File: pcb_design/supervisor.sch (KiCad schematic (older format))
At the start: 15 parts, among them U5 7400-TSSOP, U6 SN74ALVC08PWR, U7 SN74ALVC08PWR, U8 SN74AUP1G74

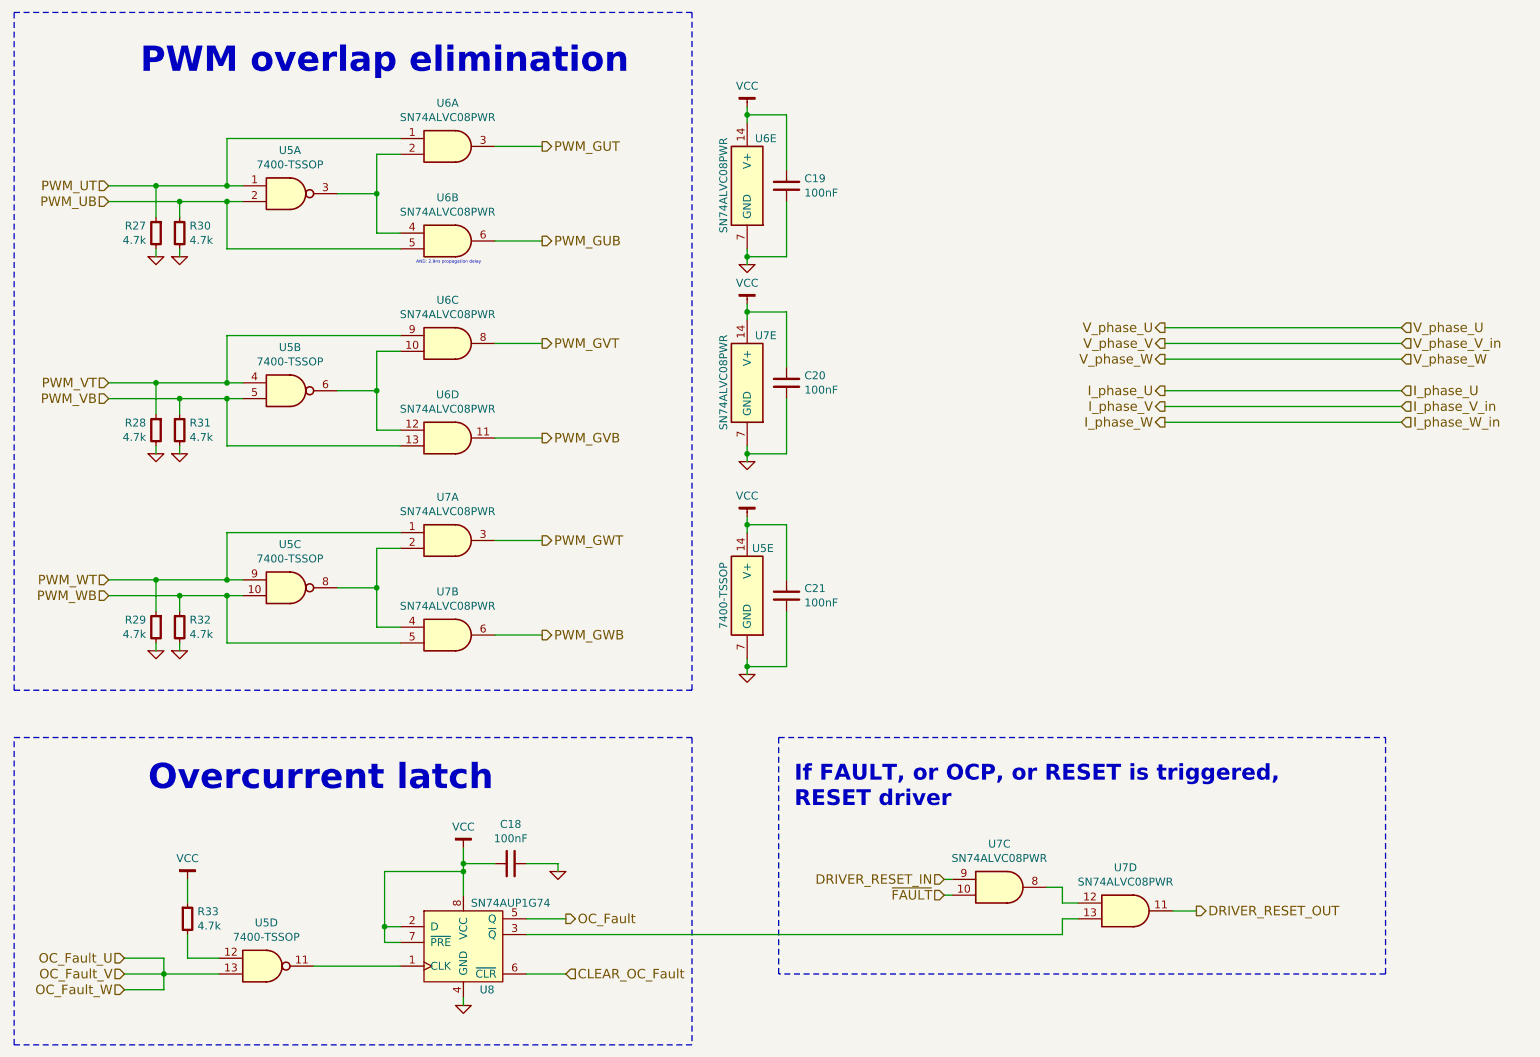
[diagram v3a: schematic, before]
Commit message: Added lp filters, fuses, tvs and power symbols
Signed-off-by: Marcos Chaparro <mchaparro@paltatech.com>
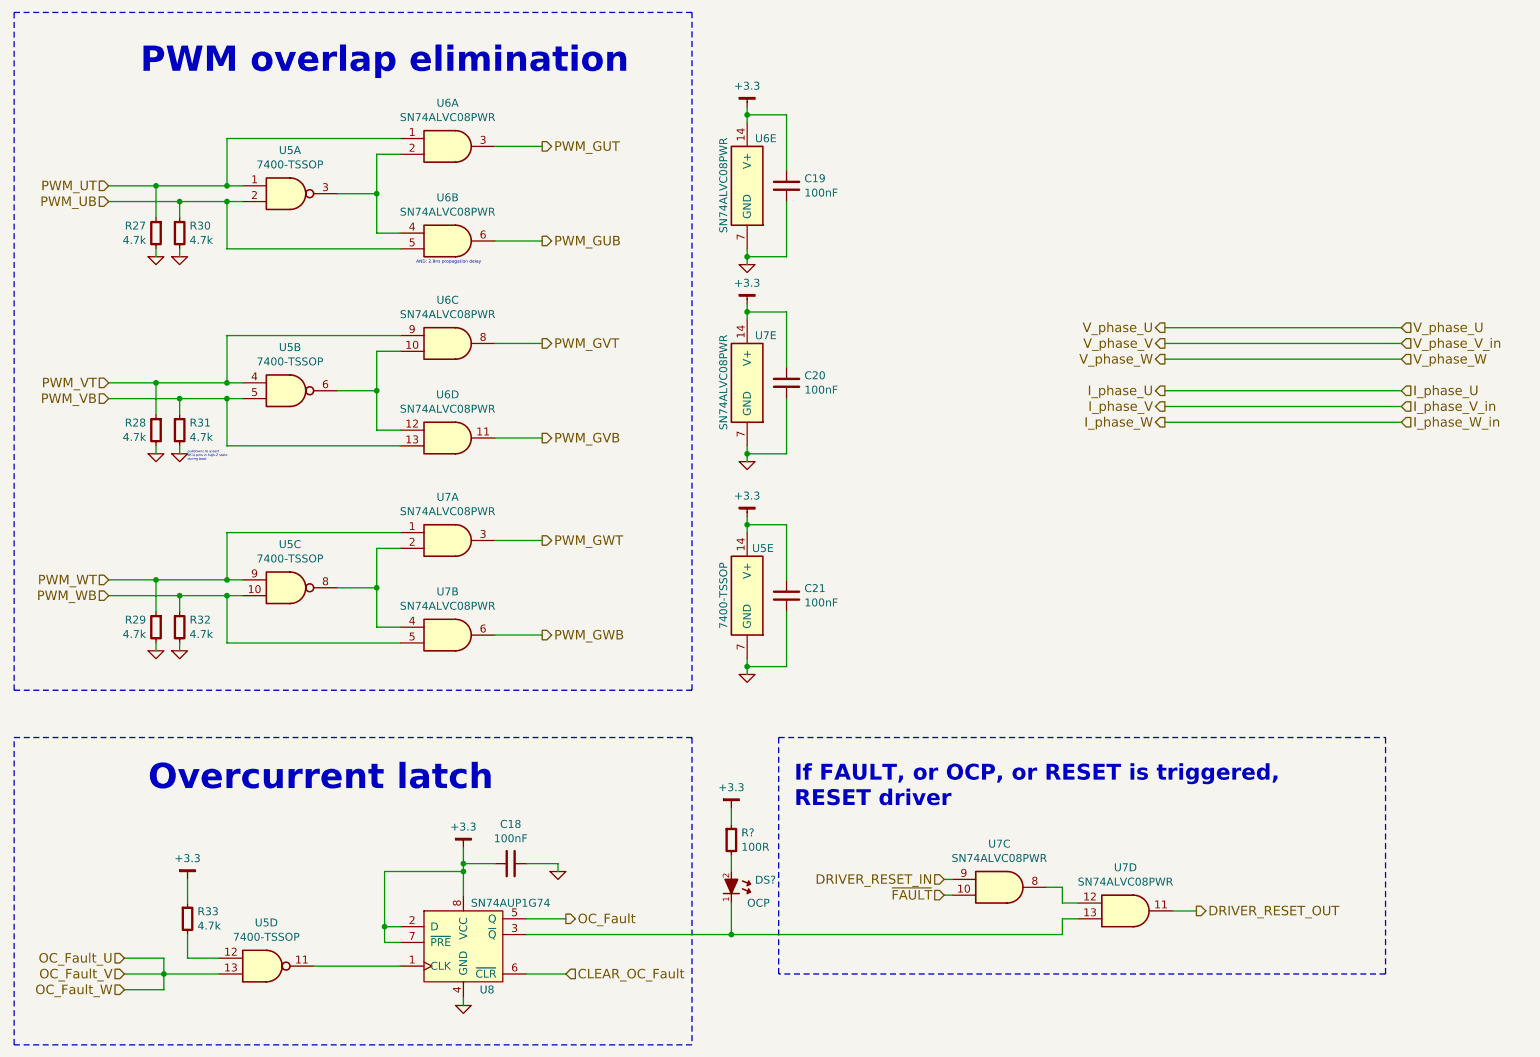
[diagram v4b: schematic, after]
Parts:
- added DS?: OCP, smd-semi:LED-0603, symbol LED-0603
- added R?: 100R, IPC7351-Nominal:RESC1608X50, symbol R-0603
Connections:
- net at U7.13 (D2D), U8.3 (~Q): now also DS?.1 (K)
- net VCC renamed +3.3
- net +3.3: now also R?.1
- new net: DS?.2 (A), R?.2
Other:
- note added: "pulldowns to assert\nMCU pins in high-Z state\nduring boot"
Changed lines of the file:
@@
 Wire Notes Line
 	5800 6950 5800 5450
-$Comp
-L VCC #PWR?
-U 1 1 588980B5
-P 3800 6150
-AR Path="/5886DA84/588980B5" Ref="#PWR?"  Part="1"
-AR Path="/588C2790/588980B5" Ref="#PWR?"  Part="1"
-AR Path="/5888D059/588980B5" Ref="#PWR76"  Part="1"
-F 0 "#PWR76" H 3800 6200 30  0001 C CNN
-F 1 "VCC" H 3800 6283 50  0000 C CNN
-F 2 "" H 3800 6150 60  0000 C CNN
-F 3 "" H 3800 6150 60  0000 C CNN
-	1    3800 6150
-	1    0    0    -1
-$EndComp
-$Comp
-L VCC #PWR?
-U 1 1 58898103
-P 2050 6350
-AR Path="/5886DA84/58898103" Ref="#PWR?"  Part="1"
-AR Path="/588C2790/58898103" Ref="#PWR?"  Part="1"
-AR Path="/5888D059/58898103" Ref="#PWR75"  Part="1"
-F 0 "#PWR75" H 2050 6400 30  0001 C CNN
-F 1 "VCC" H 2050 6483 50  0000 C CNN
-F 2 "" H 2050 6350 60  0000 C CNN
-F 3 "" H 2050 6350 60  0000 C CNN
-	1    2050 6350
-	1    0    0    -1
-$EndComp
-$Comp
-L VCC #PWR?
-U 1 1 588981CE
-P 5600 4050
-AR Path="/5886DA84/588981CE" Ref="#PWR?"  Part="1"
-AR Path="/588C2790/588981CE" Ref="#PWR?"  Part="1"
-AR Path="/5888D059/588981CE" Ref="#PWR83"  Part="1"
-F 0 "#PWR83" H 5600 4100 30  0001 C CNN
-F 1 "VCC" H 5600 4183 50  0000 C CNN
-F 2 "" H 5600 4050 60  0000 C CNN
-F 3 "" H 5600 4050 60  0000 C CNN
-	1    5600 4050
-	1    0    0    -1
-$EndComp
 Wire Wire Line
 	5600 4050 5600 4150
-$Comp
-L VCC #PWR?
-U 1 1 58898412
-P 5600 1450
-AR Path="/5886DA84/58898412" Ref="#PWR?"  Part="1"
-AR Path="/588C2790/58898412" Ref="#PWR?"  Part="1"
-AR Path="/5888D059/58898412" Ref="#PWR79"  Part="1"
-F 0 "#PWR79" H 5600 1500 30  0001 C CNN
-F 1 "VCC" H 5600 1583 50  0000 C CNN
-F 2 "" H 5600 1450 60  0000 C CNN
-F 3 "" H 5600 1450 60  0000 C CNN
-	1    5600 1450
-	1    0    0    -1
-$EndComp
 Wire Wire Line
 	5600 1450 5600 1550
-$Comp
-L VCC #PWR?
-U 1 1 588984F1
-P 5600 2700
-AR Path="/5886DA84/588984F1" Ref="#PWR?"  Part="1"
-AR Path="/588C2790/588984F1" Ref="#PWR?"  Part="1"
-AR Path="/5888D059/588984F1" Ref="#PWR81"  Part="1"
-F 0 "#PWR81" H 5600 2750 30  0001 C CNN
-F 1 "VCC" H 5600 2833 50  0000 C CNN
-F 2 "" H 5600 2700 60  0000 C CNN
-F 3 "" H 5600 2700 60  0000 C CNN
-	1    5600 2700
-	1    0    0    -1
-$EndComp
 Wire Wire Line
 	5600 2700 5600 2800
@@
 	1    0    0    -1
 $EndComp
+$Comp
+L LED-0603 DS?
+U 1 1 588B328E
+P 5500 6400
+F 0 "DS?" H 5650 6446 50  0000 L CNN
+F 1 "OCP" H 5600 6300 50  0000 L CNN
+F 2 "smd-semi:LED-0603" H -300 -550 50  0001 C CNN
+F 3 "" H -300 -400 60  0000 C CNN
+F 4 "LED RED [0603]" H -300 -650 60  0001 C CNN "BOM"
+	1    5500 6400
+	1    0    0    -1
+$EndComp
+$Comp
+L R-0603 R?
+U 1 1 588B34EA
+P 5500 6100
+F 0 "R?" H 5563 6146 50  0000 L CNN
+F 1 "100R" H 5563 6055 50  0000 L CNN
+F 2 "IPC7351-Nominal:RESC1608X50" H 5500 6100 50  0001 C CNN
+F 3 "" H 5500 6150 60  0000 C CNN
+F 4 "RES SMD 1k 5% [0603]" H 6250 6650 60  0001 C CNN "BOM"
+	1    5500 6100
+	1    0    0    -1
+$EndComp
+Wire Wire Line
+	5500 6200 5500 6300
+Wire Wire Line
+	5500 6500 5500 6700
+Connection ~ 5500 6700
+Wire Wire Line
+	5500 5900 5500 6000
+$Comp
+L +3.3 #PWR?
+U 1 1 588B453A
+P 5600 4050
+F 0 "#PWR?" H 5650 4100 30  0001 C CNN
+F 1 "+3.3" H 5600 4183 50  0000 C CNN
+F 2 "" H -950 100 60  0000 C CNN
+F 3 "" H -950 100 60  0000 C CNN
+	1    5600 4050
+	1    0    0    -1
+$EndComp
+$Comp
+L +3.3 #PWR?
+U 1 1 588B46D1
+P 5600 2700
+F 0 "#PWR?" H 5650 2750 30  0001 C CNN
+F 1 "+3.3" H 5600 2833 50  0000 C CNN
+F 2 "" H -950 -1250 60  0000 C CNN
+F 3 "" H -950 -1250 60  0000 C CNN
+	1    5600 2700
+	1    0    0    -1
+$EndComp
+$Comp
+L +3.3 #PWR?
+U 1 1 588B47E2
+P 5600 1450
+F 0 "#PWR?" H 5650 1500 30  0001 C CNN
+F 1 "+3.3" H 5600 1583 50  0000 C CNN
+F 2 "" H -950 -2500 60  0000 C CNN
+F 3 "" H -950 -2500 60  0000 C CNN
+	1    5600 1450
+	1    0    0    -1
+$EndComp
+$Comp
+L +3.3 #PWR?
+U 1 1 588B4A14
+P 5500 5900
+F 0 "#PWR?" H 5550 5950 30  0001 C CNN
+F 1 "+3.3" H 5500 6033 50  0000 C CNN
+F 2 "" H -1050 1950 60  0000 C CNN
+F 3 "" H -1050 1950 60  0000 C CNN
+	1    5500 5900
+	1    0    0    -1
+$EndComp
+$Comp
+L +3.3 #PWR?
+U 1 1 588B4BFB
+P 3800 6150
+F 0 "#PWR?" H 3850 6200 30  0001 C CNN
+F 1 "+3.3" H 3800 6283 50  0000 C CNN
+F 2 "" H -2750 2200 60  0000 C CNN
+F 3 "" H -2750 2200 60  0000 C CNN
+	1    3800 6150
+	1    0    0    -1
+$EndComp
+$Comp
+L +3.3 #PWR?
+U 1 1 588B4CB5
+P 2050 6350
+F 0 "#PWR?" H 2100 6400 30  0001 C CNN
+F 1 "+3.3" H 2050 6483 50  0000 C CNN
+F 2 "" H -4500 2400 60  0000 C CNN
+F 3 "" H -4500 2400 60  0000 C CNN
+	1    2050 6350
+	1    0    0    -1
+$EndComp
+Text Notes 2050 3700 0    15   ~ 0
+pulldowns to assert\nMCU pins in high-Z state\nduring boot
 $EndSCHEMATC

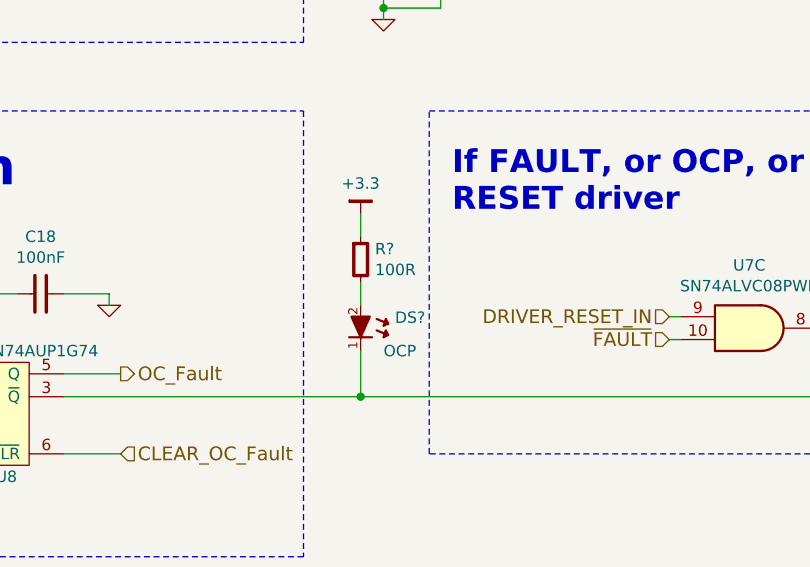
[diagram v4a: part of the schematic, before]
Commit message: Added bus voltage conditioning, %v to accel and regen inputs, regulator diode, annotated schematic
Signed-off-by: Marcos Chaparro <mchaparro@paltatech.com>
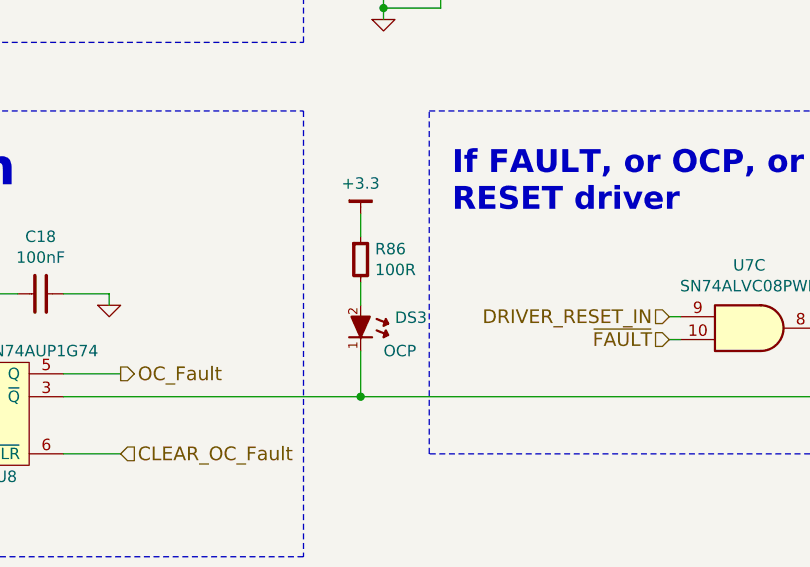
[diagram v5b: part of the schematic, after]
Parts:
- gave numbers to parts that had none: 2
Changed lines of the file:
@@
 $Descr A4 11693 8268
 encoding utf-8
-Sheet 7 12
+Sheet 7 13
 Title ""
 Date ""
@@
 Connection ~ 2000 2050
 $Comp
-L GND #PWR69
+L GND #PWR83
 U 1 1 588831C2
 P 1850 2400
-F 0 "#PWR69" H 1850 2400 30  0001 C CNN
+F 0 "#PWR83" H 1850 2400 30  0001 C CNN
 F 1 "GND" H 1850 2330 30  0001 C CNN
 F 2 "" H 1850 2400 60  0000 C CNN
@@
 	1850 2400 1850 2350
 $Comp
-L GND #PWR72
+L GND #PWR86
 U 1 1 58883201
 P 2000 2400
-F 0 "#PWR72" H 2000 2400 30  0001 C CNN
+F 0 "#PWR86" H 2000 2400 30  0001 C CNN
 F 1 "GND" H 2000 2330 30  0001 C CNN
 F 2 "" H 2000 2400 60  0000 C CNN
@@
 Connection ~ 2000 3300
 $Comp
-L GND #PWR70
+L GND #PWR84
 U 1 1 588824FD
 P 1850 3650
-F 0 "#PWR70" H 1850 3650 30  0001 C CNN
+F 0 "#PWR84" H 1850 3650 30  0001 C CNN
 F 1 "GND" H 1850 3580 30  0001 C CNN
 F 2 "" H 1850 3650 60  0000 C CNN
@@
 	1850 3650 1850 3600
 $Comp
-L GND #PWR73
+L GND #PWR87
 U 1 1 58882504
 P 2000 3650
-F 0 "#PWR73" H 2000 3650 30  0001 C CNN
+F 0 "#PWR87" H 2000 3650 30  0001 C CNN
 F 1 "GND" H 2000 3580 30  0001 C CNN
 F 2 "" H 2000 3650 60  0000 C CNN
@@
 Connection ~ 2000 4550
 $Comp
-L GND #PWR71
+L GND #PWR85
 U 1 1 5888288C
 P 1850 4900
-F 0 "#PWR71" H 1850 4900 30  0001 C CNN
+F 0 "#PWR85" H 1850 4900 30  0001 C CNN
 F 1 "GND" H 1850 4830 30  0001 C CNN
 F 2 "" H 1850 4900 60  0000 C CNN
@@
 	1850 4900 1850 4850
 $Comp
-L GND #PWR74
+L GND #PWR88
 U 1 1 58882893
 P 2000 4900
-F 0 "#PWR74" H 2000 4900 30  0001 C CNN
+F 0 "#PWR88" H 2000 4900 30  0001 C CNN
 F 1 "GND" H 2000 4830 30  0001 C CNN
 F 2 "" H 2000 4900 60  0000 C CNN
@@
 $EndComp
 $Comp
-L GND #PWR77
+L GND #PWR91
 U 1 1 5888A11E
 P 3800 7150
-F 0 "#PWR77" H 3800 7150 30  0001 C CNN
+F 0 "#PWR91" H 3800 7150 30  0001 C CNN
 F 1 "GND" H 3800 7080 30  0001 C CNN
 F 2 "" H 3800 7150 60  0000 C CNN
@@
 	4400 6250 4400 6300
 $Comp
-L GND #PWR78
+L GND #PWR92
 U 1 1 5888A46C
 P 4400 6300
-F 0 "#PWR78" H 4400 6300 30  0001 C CNN
+F 0 "#PWR92" H 4400 6300 30  0001 C CNN
 F 1 "GND" H 4400 6230 30  0001 C CNN
 F 2 "" H 4400 6300 60  0000 C CNN
@@
 	5600 4950 5600 5050
 $Comp
-L GND #PWR84
+L GND #PWR99
 U 1 1 58899228
 P 5600 5050
-F 0 "#PWR84" H 5600 5050 30  0001 C CNN
+F 0 "#PWR99" H 5600 5050 30  0001 C CNN
 F 1 "GND" H 5600 4980 30  0001 C CNN
 F 2 "" H 5600 5050 60  0000 C CNN
@@
 Connection ~ 5600 5000
 $Comp
-L GND #PWR82
+L GND #PWR97
 U 1 1 5889937C
 P 5600 3700
-F 0 "#PWR82" H 5600 3700 30  0001 C CNN
+F 0 "#PWR97" H 5600 3700 30  0001 C CNN
 F 1 "GND" H 5600 3630 30  0001 C CNN
 F 2 "" H 5600 3700 60  0000 C CNN
@@
 $EndComp
 $Comp
-L GND #PWR80
+L GND #PWR95
 U 1 1 588993D2
 P 5600 2450
-F 0 "#PWR80" H 5600 2450 30  0001 C CNN
+F 0 "#PWR95" H 5600 2450 30  0001 C CNN
 F 1 "GND" H 5600 2380 30  0001 C CNN
 F 2 "" H 5600 2450 60  0000 C CNN
@@
 $EndComp
 $Comp
-L LED-0603 DS?
+L LED-0603 DS3
 U 1 1 588B328E
 P 5500 6400
-F 0 "DS?" H 5650 6446 50  0000 L CNN
+F 0 "DS3" H 5650 6446 50  0000 L CNN
 F 1 "OCP" H 5600 6300 50  0000 L CNN
 F 2 "smd-semi:LED-0603" H -300 -550 50  0001 C CNN
@@
 $EndComp
 $Comp
-L R-0603 R?
+L R-0603 R86
 U 1 1 588B34EA
 P 5500 6100
-F 0 "R?" H 5563 6146 50  0000 L CNN
+F 0 "R86" H 5563 6146 50  0000 L CNN
 F 1 "100R" H 5563 6055 50  0000 L CNN
 F 2 "IPC7351-Nominal:RESC1608X50" H 5500 6100 50  0001 C CNN
@@
 	5500 5900 5500 6000
 $Comp
-L +3.3 #PWR?
+L +3.3 #PWR98
 U 1 1 588B453A
 P 5600 4050
-F 0 "#PWR?" H 5650 4100 30  0001 C CNN
+F 0 "#PWR98" H 5650 4100 30  0001 C CNN
 F 1 "+3.3" H 5600 4183 50  0000 C CNN
 F 2 "" H -950 100 60  0000 C CNN
@@
 $EndComp
 $Comp
-L +3.3 #PWR?
+L +3.3 #PWR96
 U 1 1 588B46D1
 P 5600 2700
-F 0 "#PWR?" H 5650 2750 30  0001 C CNN
+F 0 "#PWR96" H 5650 2750 30  0001 C CNN
 F 1 "+3.3" H 5600 2833 50  0000 C CNN
 F 2 "" H -950 -1250 60  0000 C CNN
@@
 $EndComp
 $Comp
-L +3.3 #PWR?
+L +3.3 #PWR94
 U 1 1 588B47E2
 P 5600 1450
-F 0 "#PWR?" H 5650 1500 30  0001 C CNN
+F 0 "#PWR94" H 5650 1500 30  0001 C CNN
 F 1 "+3.3" H 5600 1583 50  0000 C CNN
 F 2 "" H -950 -2500 60  0000 C CNN
@@
 $EndComp
 $Comp
-L +3.3 #PWR?
+L +3.3 #PWR93
 U 1 1 588B4A14
 P 5500 5900
-F 0 "#PWR?" H 5550 5950 30  0001 C CNN
+F 0 "#PWR93" H 5550 5950 30  0001 C CNN
 F 1 "+3.3" H 5500 6033 50  0000 C CNN
 F 2 "" H -1050 1950 60  0000 C CNN
@@
 $EndComp
 $Comp
-L +3.3 #PWR?
+L +3.3 #PWR90
 U 1 1 588B4BFB
 P 3800 6150
-F 0 "#PWR?" H 3850 6200 30  0001 C CNN
+F 0 "#PWR90" H 3850 6200 30  0001 C CNN
 F 1 "+3.3" H 3800 6283 50  0000 C CNN
 F 2 "" H -2750 2200 60  0000 C CNN
@@
 $EndComp
 $Comp
-L +3.3 #PWR?
+L +3.3 #PWR89
 U 1 1 588B4CB5
 P 2050 6350
-F 0 "#PWR?" H 2100 6400 30  0001 C CNN
+F 0 "#PWR89" H 2100 6400 30  0001 C CNN
 F 1 "+3.3" H 2050 6483 50  0000 C CNN
 F 2 "" H -4500 2400 60  0000 C CNN
